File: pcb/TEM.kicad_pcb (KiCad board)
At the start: 2 copper layers, 36 x 15 mm, 23 parts, among them J1 Conn_01x04_Pin, SW1 SW_Wuerth_450301014042, U1 AT24CM02-SSHM, U2 AT24CM02-SSHM

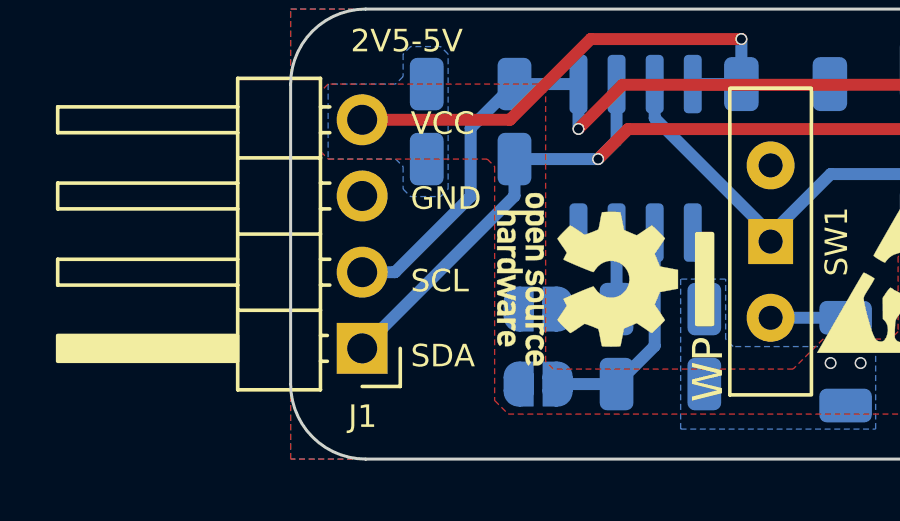
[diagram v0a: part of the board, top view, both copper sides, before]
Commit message: Swapped SCL/SDA
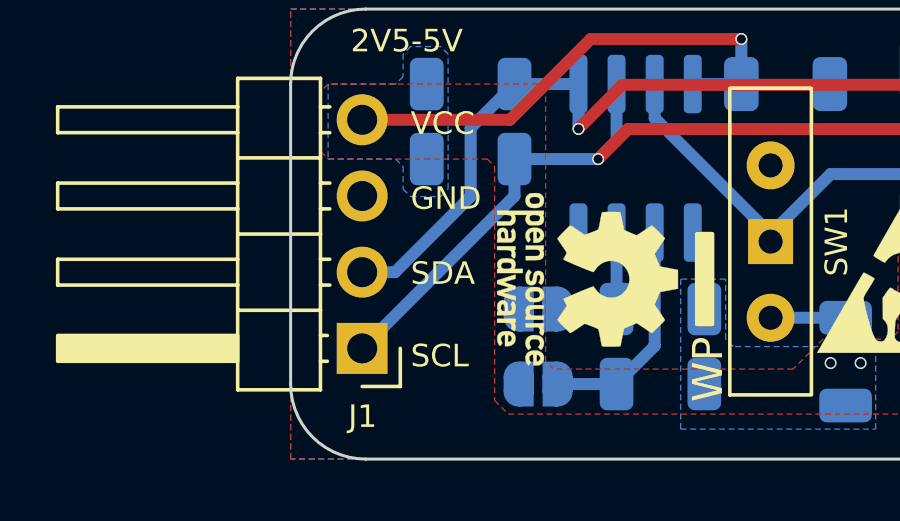
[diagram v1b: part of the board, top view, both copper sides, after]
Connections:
- J1 pad 1: SDA -> SCL
- J1 pad 2: SCL -> SDA
- R4 pad 2: SDA -> SCL
- R5 pad 2: SCL -> SDA
- U1 pad 5: SCL -> SDA
- U1 pad 6: SDA -> SCL
- U2 pad 5: SCL -> SDA
- U2 pad 6: SDA -> SCL
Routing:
- net SDA: track 31.4 -> 28.2 mm
- net SCL: track 28.2 -> 31.4 mm
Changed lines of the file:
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@@
 		(property ki_fp_filters "Fiducial*")
 		(sheetname "/")
-		(sheetfile "PROM.kicad_sch")
+		(sheetfile "TEM.kicad_sch")
 		(attr smd)
 		(fp_poly
@@
 		(property ki_fp_filters "Connector*:*_1x??_*")
 		(sheetname "/")
-		(sheetfile "PROM.kicad_sch")
+		(sheetfile "TEM.kicad_sch")
 		(attr through_hole)
 		(fp_line
@@
 			(layers "*.Cu" "*.Mask")
 			(remove_unused_layers no)
-			(net 3 "SDA")
+			(net 4 "SCL")
 			(pinfunction "Pin_1")
 			(pintype "passive")
@@
 			(layers "*.Cu" "*.Mask")
 			(remove_unused_layers no)
-			(net 4 "SCL")
+			(net 3 "SDA")
 			(pinfunction "Pin_2")
 			(pintype "passive")
@@
 		(property ki_fp_filters "Fiducial*")
 		(sheetname "/")
-		(sheetfile "PROM.kicad_sch")
+		(sheetfile "TEM.kicad_sch")
 		(attr exclude_from_pos_files allow_missing_courtyard)
 		(fp_poly
@@
 		(property ki_fp_filters "Fiducial*")
 		(sheetname "/")
-		(sheetfile "PROM.kicad_sch")
+		(sheetfile "TEM.kicad_sch")
 		(attr exclude_from_pos_files allow_missing_courtyard)
 		(fp_poly
@@
 		(property ki_fp_filters "MountingHole*Pad*")
 		(sheetname "/")
-		(sheetfile "PROM.kicad_sch")
+		(sheetfile "TEM.kicad_sch")
 		(attr exclude_from_pos_files exclude_from_bom)
 		(fp_circle
@@
 		(property ki_fp_filters "Fiducial*")
 		(sheetname "/")
-		(sheetfile "PROM.kicad_sch")
+		(sheetfile "TEM.kicad_sch")
 		(attr exclude_from_pos_files)
 		(fp_poly
@@
 		(property ki_fp_filters "SW*Wuerth*WS*SLTV*10x2.5x6.4*P2.54mm*")
 		(sheetname "/")
-		(sheetfile "PROM.kicad_sch")
+		(sheetfile "TEM.kicad_sch")
 		(attr through_hole)
 		(fp_rect
@@
 		(property ki_fp_filters "SOIC*3.9x4.9mm*P1.27mm*")
 		(sheetname "/")
-		(sheetfile "PROM.kicad_sch")
+		(sheetfile "TEM.kicad_sch")
 		(attr smd)
 		(fp_line
@@
 			(layers "B.Cu" "B.Mask" "B.Paste")
 			(roundrect_rratio 0.25)
-			(net 4 "SCL")
+			(net 3 "SDA")
 			(pinfunction "SDA")
 			(pintype "bidirectional")
@@
 			(layers "B.Cu" "B.Mask" "B.Paste")
 			(roundrect_rratio 0.25)
-			(net 3 "SDA")
+			(net 4 "SCL")
 			(pinfunction "SCL")
 			(pintype "input")
@@
 		(property ki_fp_filters "SOIC*3.9x4.9mm*P1.27mm*")
 		(sheetname "/")
-		(sheetfile "PROM.kicad_sch")
+		(sheetfile "TEM.kicad_sch")
 		(attr smd)
 		(fp_line
@@
 			(layers "B.Cu" "B.Mask" "B.Paste")
 			(roundrect_rratio 0.25)
-			(net 4 "SCL")
+			(net 3 "SDA")
 			(pinfunction "SDA")
 			(pintype "bidirectional")
@@
 			(layers "B.Cu" "B.Mask" "B.Paste")
 			(roundrect_rratio 0.25)
-			(net 3 "SDA")
+			(net 4 "SCL")
 			(pinfunction "SCL")
 			(pintype "input")
@@
 		(property ki_fp_filters "R_*")
 		(sheetname "/")
-		(sheetfile "PROM.kicad_sch")
+		(sheetfile "TEM.kicad_sch")
 		(attr smd)
 		(fp_line
@@
 			(layers "B.Cu" "B.Mask" "B.Paste")
 			(roundrect_rratio 0.222222)
-			(net 3 "SDA")
+			(net 4 "SCL")
 			(pintype "passive")
 		)
@@
 		(property ki_fp_filters "R_*")
 		(sheetname "/")
-		(sheetfile "PROM.kicad_sch")
+		(sheetfile "TEM.kicad_sch")
 		(attr smd)
 		(fp_line
@@
 		(property ki_fp_filters "C_*")
 		(sheetname "/")
-		(sheetfile "PROM.kicad_sch")
+		(sheetfile "TEM.kicad_sch")
 		(attr smd)
 		(fp_line
@@
 		(property ki_fp_filters "C_*")
 		(sheetname "/")
-		(sheetfile "PROM.kicad_sch")
+		(sheetfile "TEM.kicad_sch")
 		(attr smd)
 		(fp_line
@@
 		(property ki_fp_filters "SolderJumper*Open*")
 		(sheetname "/")
-		(sheetfile "PROM.kicad_sch")
+		(sheetfile "TEM.kicad_sch")
 		(zone_connect 1)
 		(attr exclude_from_pos_files exclude_from_bom allow_soldermask_bridges)
@@
 		(property ki_fp_filters "R_*")
 		(sheetname "/")
-		(sheetfile "PROM.kicad_sch")
+		(sheetfile "TEM.kicad_sch")
 		(attr smd)
 		(fp_line
@@
 		(property ki_fp_filters "SolderJumper*Open*")
 		(sheetname "/")
-		(sheetfile "PROM.kicad_sch")
+		(sheetfile "TEM.kicad_sch")
 		(zone_connect 1)
 		(attr exclude_from_pos_files exclude_from_bom allow_soldermask_bridges)
@@
 		(property ki_fp_filters "CP_*")
 		(sheetname "/")
-		(sheetfile "PROM.kicad_sch")
+		(sheetfile "TEM.kicad_sch")
 		(attr smd)
 		(fp_line
@@
 		(property ki_fp_filters "R_*")
 		(sheetname "/")
-		(sheetfile "PROM.kicad_sch")
+		(sheetfile "TEM.kicad_sch")
 		(attr smd)
 		(fp_line
@@
 		(property ki_fp_filters "SolderJumper*Open*")
 		(sheetname "/")
-		(sheetfile "PROM.kicad_sch")
+		(sheetfile "TEM.kicad_sch")
 		(zone_connect 1)
 		(attr exclude_from_pos_files exclude_from_bom allow_soldermask_bridges)
@@
 		(property ki_fp_filters "R_*")
 		(sheetname "/")
-		(sheetfile "PROM.kicad_sch")
+		(sheetfile "TEM.kicad_sch")
 		(attr smd)
 		(fp_line
@@
 		(property ki_fp_filters "SolderJumper*Open*")
 		(sheetname "/")
-		(sheetfile "PROM.kicad_sch")
+		(sheetfile "TEM.kicad_sch")
 		(zone_connect 1)
 		(attr exclude_from_pos_files exclude_from_bom allow_soldermask_bridges)
@@
 		(property ki_fp_filters "R_*")
 		(sheetname "/")
-		(sheetfile "PROM.kicad_sch")
+		(sheetfile "TEM.kicad_sch")
 		(attr smd)
 		(fp_line
@@
 		(property ki_fp_filters "R_*")
 		(sheetname "/")
-		(sheetfile "PROM.kicad_sch")
+		(sheetfile "TEM.kicad_sch")
 		(attr smd)
 		(fp_line
@@
 			(layers "B.Cu" "B.Mask" "B.Paste")
 			(roundrect_rratio 0.222222)
-			(net 4 "SCL")
+			(net 3 "SDA")
 			(pintype "passive")
 		)
@@
 		)
 	)
-	(gr_text "SCL"
-		(at 119 84.5 0)
+	(gr_text "SDA"
+		(at 119 84.25 0)
 		(layer "F.SilkS")
 		(effects
@@
 		)
 	)
-	(gr_text "SDA"
+	(gr_text "SCL"
 		(at 119 87 0)
 		(layer "F.SilkS")
@@
 	)
 	(segment
-		(start 126.25 79)
-		(end 140.76 79)
+		(start 124.595 78.995)
+		(end 126.065 77.525)
 		(width 0.4)
 		(layer "F.Cu")
@@
 	)
 	(segment
-		(start 125.25 80)
-		(end 126.25 79)
+		(start 126.065 77.525)
+		(end 138.75 77.525)
 		(width 0.4)
 		(layer "F.Cu")
@@
 	)
 	(via
-		(at 140.76 79)
+		(at 138.75 77.525)
 		(size 0.4)
 		(drill 0.3)
@@
 	)
 	(via
-		(at 125.25 80)
+		(at 124.595 78.995)
 		(size 0.4)
 		(drill 0.3)
@@
 	)
 	(segment
-		(start 140.76 79)
-		(end 140.76 77.525)
+		(start 122.4625 77.5)
+		(end 124.595 77.5)
 		(width 0.4)
 		(layer "B.Cu")
@@
 	)
 	(segment
-		(start 125.25 80)
-		(end 125.865 79.385)
+		(start 139.49 77.525)
+		(end 138.75 77.525)
 		(width 0.4)
 		(layer "B.Cu")
@@
 	)
 	(segment
-		(start 122.4625 80)
-		(end 122.4625 81.2325)
+		(start 118.48 83.77)
+		(end 117.385 83.77)
 		(width 0.4)
 		(layer "B.Cu")
@@
 	)
 	(segment
-		(start 122.4625 80)
-		(end 125.25 80)
+		(start 124.595 77.5)
+		(end 124.595 78.995)
 		(width 0.4)
 		(layer "B.Cu")
@@
 	)
 	(segment
-		(start 125.865 79.385)
-		(end 125.865 77.5)
+		(start 122.4625 77.5)
+		(end 121 78.9625)
 		(width 0.4)
 		(layer "B.Cu")
@@
 	)
 	(segment
-		(start 122.4625 81.2325)
-		(end 117.385 86.31)
+		(start 139.465 77.5)
+		(end 139.49 77.525)
 		(width 0.4)
 		(layer "B.Cu")
@@
 	)
 	(segment
-		(start 124.595 78.995)
-		(end 126.065 77.525)
+		(start 121 81.25)
+		(end 118.48 83.77)
+		(width 0.4)
+		(layer "B.Cu")
+		(net 3)
+	)
+	(segment
+		(start 121 78.9625)
+		(end 121 81.25)
+		(width 0.4)
+		(layer "B.Cu")
+		(net 3)
+	)
+	(segment
+		(start 126.25 79)
+		(end 140.76 79)
 		(width 0.4)
 		(layer "F.Cu")
@@
 	)
 	(segment
-		(start 126.065 77.525)
-		(end 138.75 77.525)
+		(start 125.25 80)
+		(end 126.25 79)
 		(width 0.4)
 		(layer "F.Cu")
@@
 	)
 	(via
-		(at 138.75 77.525)
+		(at 140.76 79)
 		(size 0.4)
 		(drill 0.3)
@@
 	)
 	(via
-		(at 124.595 78.995)
+		(at 125.25 80)
 		(size 0.4)
 		(drill 0.3)
@@
 	)
 	(segment
-		(start 122.4625 77.5)
-		(end 124.595 77.5)
-		(width 0.4)
-		(layer "B.Cu")
-		(net 4)
-	)
-	(segment
-		(start 139.49 77.525)
-		(end 138.75 77.525)
-		(width 0.4)
-		(layer "B.Cu")
-		(net 4)
-	)
-	(segment
-		(start 118.48 83.77)
-		(end 117.385 83.77)
+		(start 140.76 79)
+		(end 140.76 77.525)
 		(width 0.4)
 		(layer "B.Cu")
@@
 	)
 	(segment
-		(start 124.595 77.5)
-		(end 124.595 78.995)
+		(start 125.25 80)
+		(end 125.865 79.385)
 		(width 0.4)
 		(layer "B.Cu")
@@
 	)
 	(segment
-		(start 122.4625 77.5)
-		(end 121 78.9625)
+		(start 122.4625 80)
+		(end 122.4625 81.2325)
 		(width 0.4)
 		(layer "B.Cu")
@@
 	)
 	(segment
-		(start 139.465 77.5)
-		(end 139.49 77.525)
+		(start 122.4625 80)
+		(end 125.25 80)
 		(width 0.4)
 		(layer "B.Cu")
@@
 	)
 	(segment
-		(start 121 81.25)
-		(end 118.48 83.77)
+		(start 125.865 79.385)
+		(end 125.865 77.5)
 		(width 0.4)
 		(layer "B.Cu")
@@
 	)
 	(segment
-		(start 121 78.9625)
-		(end 121 81.25)
+		(start 122.4625 81.2325)
+		(end 117.385 86.31)
 		(width 0.4)
 		(layer "B.Cu")

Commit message: Adapt vendors on partlist
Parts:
- R4, R5: value n.B. -> 3k3
